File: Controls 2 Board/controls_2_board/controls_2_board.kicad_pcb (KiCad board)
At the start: 2 copper layers, 66 x 50 mm, 16 parts, among them J1 Conn_01x05_Socket, J2 Conn_01x04_Socket, J3 Conn_01x02_Socket, U1 UA741CDR, U2 MCP47CVB22-E/UN

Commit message: Just looking
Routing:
- net +3V3: track 40.4 -> 38.8 mm
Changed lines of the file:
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@@
 		(tags "Resistor Axial_DIN0204 series Axial Horizontal pin pitch 7.62mm 0.167W length 3.6mm diameter 1.6mm")
 		(property "Reference" "R2"
-			(at 3.81 1.81973 360)
+			(at 3.81 1.81973 0)
 			(layer "F.SilkS")
 			(effects
@@
 		)
 		(property "Value" "10k"
-			(at 3.81 1.92 360)
+			(at 3.81 1.92 0)
 			(layer "F.Fab")
 			(hide yes)
@@
 		)
 		(fp_text user "${REFERENCE}"
-			(at 3.81 0 360)
+			(at 3.81 0 0)
 			(layer "F.Fab")
 			(effects
@@
 		(tags "Resistor Axial_DIN0204 series Axial Horizontal pin pitch 7.62mm 0.167W length 3.6mm diameter 1.6mm")
 		(property "Reference" "R4"
-			(at 3.81 1.75 360)
+			(at 3.81 1.75 0)
 			(layer "F.SilkS")
 			(effects
@@
 		)
 		(property "Value" "30k"
-			(at 3.81 1.92 360)
+			(at 3.81 1.92 0)
 			(layer "F.Fab")
 			(hide yes)
@@
 		)
 		(fp_text user "${REFERENCE}"
-			(at 3.81 0 360)
+			(at 3.81 0 0)
 			(layer "F.Fab")
 			(effects
@@
 		(tags "Resistor Axial_DIN0204 series Axial Horizontal pin pitch 7.62mm 0.167W length 3.6mm diameter 1.6mm")
 		(property "Reference" "R3"
-			(at 3.81 2 360)
+			(at 3.81 2 0)
 			(layer "F.SilkS")
 			(effects
@@
 		)
 		(property "Value" "30k"
-			(at 6.31 1.75 360)
+			(at 6.31 1.75 0)
 			(layer "F.Fab")
 			(hide yes)
@@
 		)
 		(fp_text user "${REFERENCE}"
-			(at 3.81 0 360)
+			(at 3.81 0 0)
 			(layer "F.Fab")
 			(effects
@@
 	)
 	(segment
-		(start 132.75 83.25)
-		(end 140.5 83.25)
+		(start 137.75 83.25)
+		(end 141.25 79.75)
 		(width 0.5)
 		(layer "F.Cu")
@@
 	)
 	(segment
-		(start 141.25 66.69)
-		(end 136.75 62.19)
+		(start 132.75 83.25)
+		(end 137.75 83.25)
 		(width 0.5)
 		(layer "F.Cu")
@@
 	)
 	(segment
-		(start 140.5 83.25)
-		(end 141.25 82.5)
+		(start 141.25 79.75)
+		(end 141.25 66.69)
 		(width 0.5)
 		(layer "F.Cu")
@@
 	)
 	(segment
-		(start 141.25 82.5)
-		(end 141.25 66.69)
+		(start 141.25 66.69)
+		(end 136.75 62.19)
 		(width 0.5)
 		(layer "F.Cu")

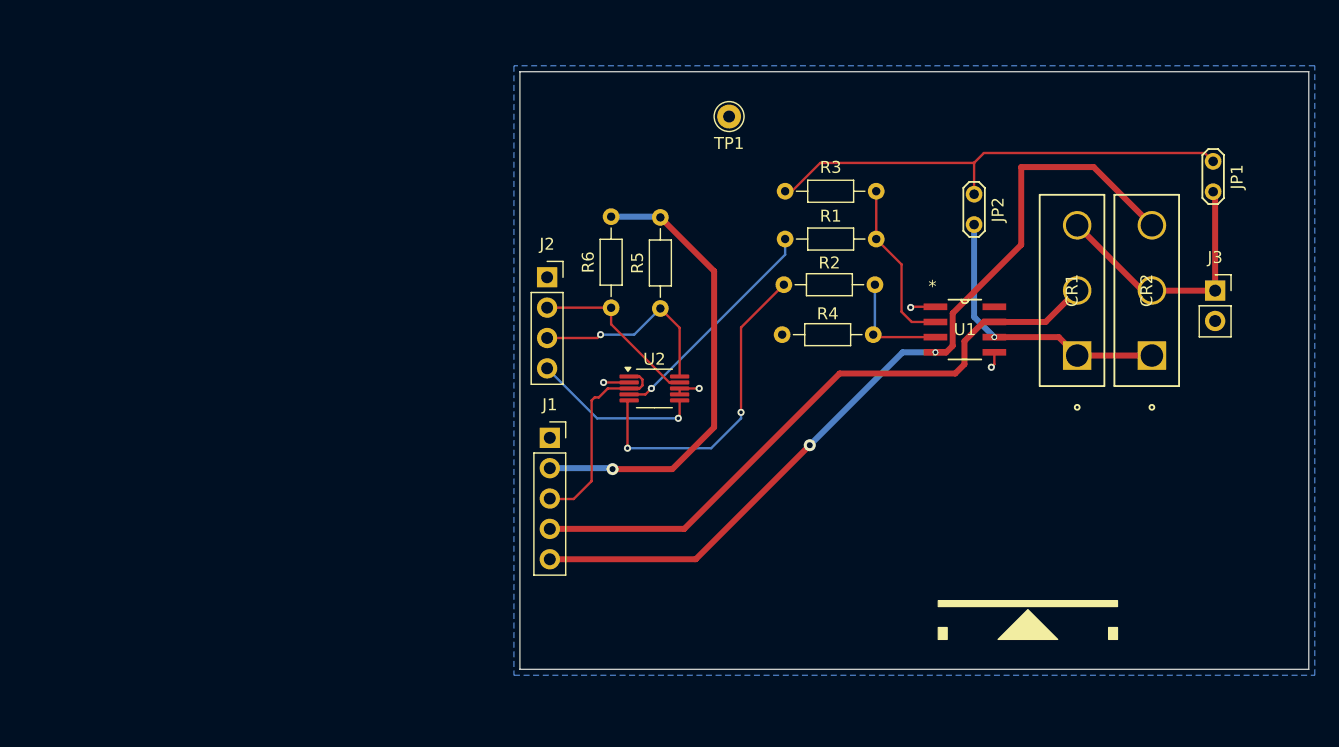
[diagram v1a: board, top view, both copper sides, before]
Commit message: Added pico
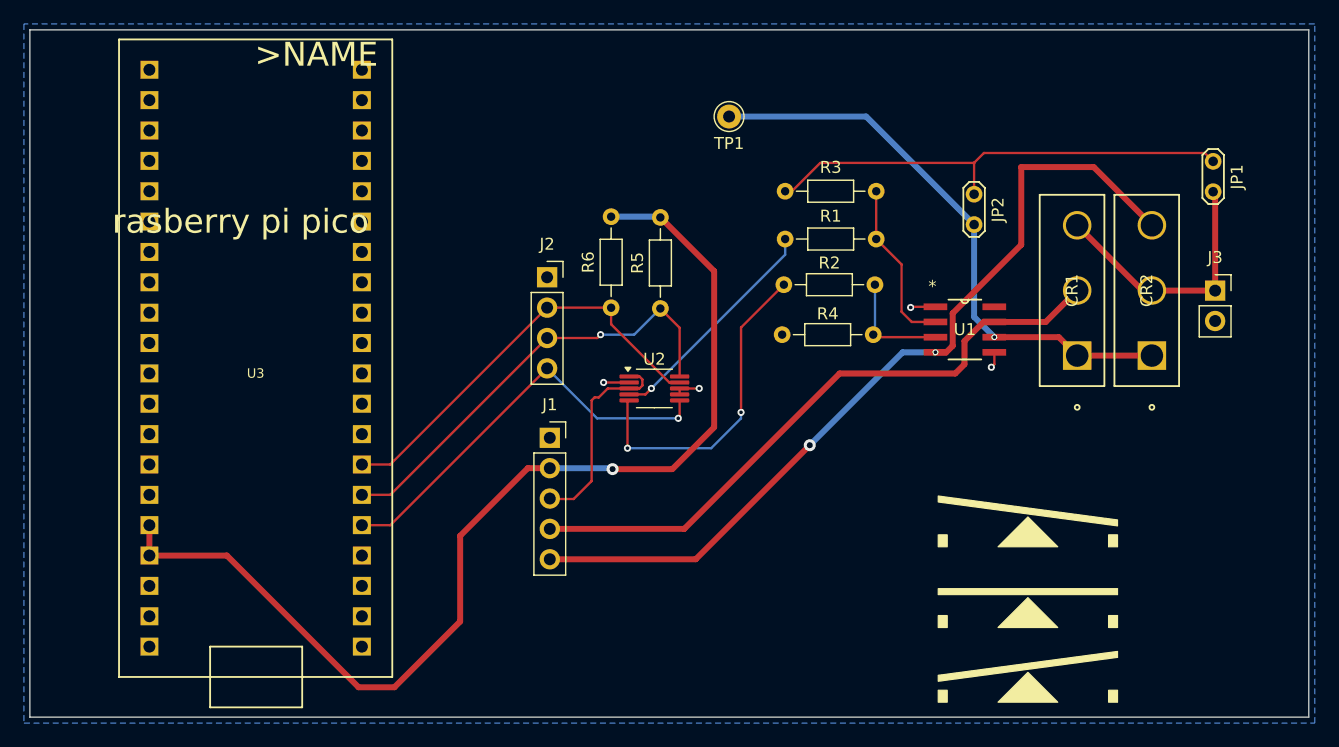
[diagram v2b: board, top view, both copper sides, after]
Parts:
- added U3: RASPBERRY_PI_PICO, Custom:RASPBERRY_PI_PICO, F.Cu at (102.9, 75.2)
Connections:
- TP1 pad 1: unconnected-(TP1-Pad1) -> Net-(JP2-B)
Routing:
- net +3V3: track 38.8 -> 91.2 mm
- net Net-(JP2-B): track 24.7 -> 48.9 mm
- net /SDA: track 16.9 -> 37.8 mm
- net /~{LAT}: track 14.3 -> 35.2 mm
- net /SCL: track 14.5 -> 35.4 mm
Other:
- board size 66 x 50 mm -> 107 x 57.5 mm
